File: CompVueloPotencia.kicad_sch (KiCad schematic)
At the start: 2 parts, among them U1 ESP32-S3-WROOM-1

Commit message: another test of updates
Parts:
- added SW1: SW_Push, symbol Switch:SW_Push
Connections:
- net EN: now reaches R1.1
- net EN: now also SW1.2
- net GND: now reaches R1.2
- new net +3V3: SW1.1
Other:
- moved on the sheet: R1

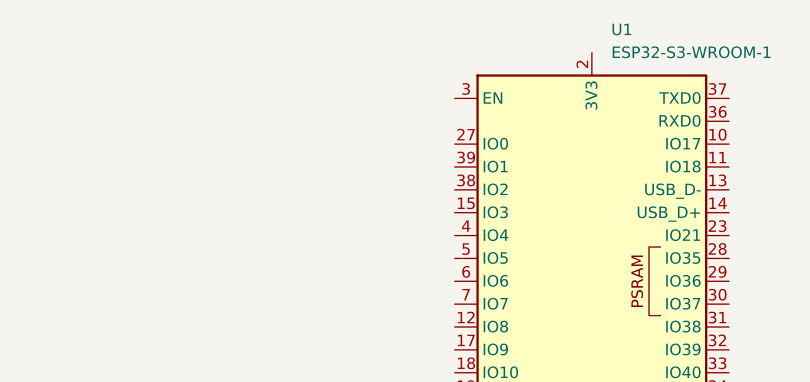
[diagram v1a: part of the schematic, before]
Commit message: last test for updates, only add to gitignore the prl file
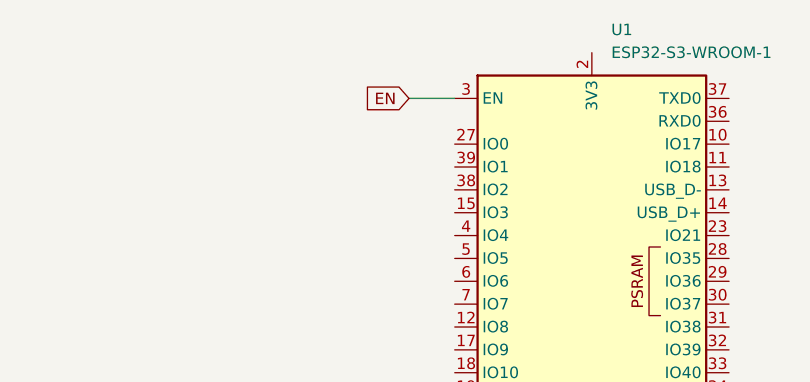
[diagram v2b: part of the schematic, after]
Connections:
- net EN: now also U1.3 (EN)
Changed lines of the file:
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@@
+	(wire
+		(pts
+			(xy 180.34 45.72) (xy 185.42 45.72)
+		)
+		(stroke
+			(width 0)
+			(type default)
+		)
+	)
 	(wire
 		(pts
@@
 		)
 	)
+	(global_label "EN"
+		(shape input)
+		(at 180.34 45.72 180)
+		(fields_autoplaced yes)
+		(effects
+			(font
+				(size 1.27 1.27)
+			)
+			(justify right)
+		)
+		(property "Intersheetrefs" "${INTERSHEET_REFS}"
+			(at 174.8753 45.72 0)
+			(effects
+				(font
+					(size 1.27 1.27)
+				)
+				(justify right)
+				(hide yes)
+			)
+		)
+	)

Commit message: little changes
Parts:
- added C1: .1uF, symbol Device:C_Small
- R1: value R_Small -> 10K
- SW1: value SW_Push -> Reset
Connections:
- net +3V3 is gone; now on net GND: SW1.1
- net GND: now also C1.2; no longer R1.2
- net EN renamed ESP32_EN
- net ESP32_EN: now also R1.2, C1.1; no longer R1.1
- new net +3.3V: R1.1
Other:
- moved on the sheet: R1, SW1
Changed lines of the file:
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@@
 	(paper "A4")
 	(junction
-		(at 80.01 57.15)
+		(at 44.45 48.26)
 		(diameter 0)
 		(color 0 0 0 0)
 	)
-	(wire
-		(pts
-			(xy 80.01 57.15) (xy 80.01 59.69)
-		)
-		(stroke
-			(width 0)
-			(type default)
-		)
-	)
-	(wire
-		(pts
-			(xy 69.85 57.15) (xy 64.77 57.15)
-		)
-		(stroke
-			(width 0)
-			(type default)
-		)
-	)
-	(wire
-		(pts
-			(xy 80.01 64.77) (xy 80.01 66.04)
-		)
-		(stroke
-			(width 0)
-			(type default)
-		)
-	)
-	(wire
-		(pts
-			(xy 64.77 57.15) (xy 64.77 50.8)
+	(junction
+		(at 49.53 39.37)
+		(diameter 0)
+		(color 0 0 0 0)
+	)
+	(junction
+		(at 44.45 39.37)
+		(diameter 0)
+		(color 0 0 0 0)
+	)
+	(wire
+		(pts
+			(xy 49.53 39.37) (xy 54.61 39.37)
+		)
+		(stroke
+			(width 0)
+			(type default)
+		)
+	)
+	(wire
+		(pts
+			(xy 49.53 36.83) (xy 49.53 39.37)
+		)
+		(stroke
+			(width 0)
+			(type default)
+		)
+	)
+	(wire
+		(pts
+			(xy 44.45 39.37) (xy 44.45 41.91)
+		)
+		(stroke
+			(width 0)
+			(type default)
+		)
+	)
+	(wire
+		(pts
+			(xy 44.45 46.99) (xy 44.45 48.26)
+		)
+		(stroke
+			(width 0)
+			(type default)
+		)
+	)
+	(wire
+		(pts
+			(xy 49.53 26.67) (xy 49.53 31.75)
+		)
+		(stroke
+			(width 0)
+			(type default)
+		)
+	)
+	(wire
+		(pts
+			(xy 44.45 48.26) (xy 33.02 48.26)
+		)
+		(stroke
+			(width 0)
+			(type default)
+		)
+	)
+	(wire
+		(pts
+			(xy 44.45 52.07) (xy 44.45 48.26)
+		)
+		(stroke
+			(width 0)
+			(type default)
+		)
+	)
+	(wire
+		(pts
+			(xy 34.29 39.37) (xy 33.02 39.37)
+		)
+		(stroke
+			(width 0)
+			(type default)
+		)
+	)
+	(wire
+		(pts
+			(xy 33.02 39.37) (xy 33.02 48.26)
 		)
 		(stroke
@@
 	(wire
 		(pts
-			(xy 80.01 57.15) (xy 90.17 57.15)
-		)
-		(stroke
-			(width 0)
-			(type default)
-		)
-	)
-	(global_label "EN"
+			(xy 44.45 39.37) (xy 49.53 39.37)
+		)
+		(stroke
+			(width 0)
+			(type default)
+		)
+	)
+	(global_label "ESP32_EN"
 		(shape input)
 		(at 180.34 45.72 180)
@@
 		)
 		(property "Intersheetrefs" "${INTERSHEET_REFS}"
-			(at 174.8753 45.72 0)
+			(at 167.8602 45.72 0)
 			(effects
 				(font
@@
 		)
 	)
-	(global_label "EN"
+	(global_label "ESP32_EN"
 		(shape input)
-		(at 90.17 57.15 0)
+		(at 54.61 39.37 0)
 		(fields_autoplaced yes)
 		(effects
@@
 		)
 		(property "Intersheetrefs" "${INTERSHEET_REFS}"
-			(at 95.6347 57.15 0)
+			(at 67.0898 39.37 0)
 			(effects
 				(font
@@
 	(symbol
 		(lib_id "power:GND")
-		(at 80.01 66.04 0)
+		(at 44.45 52.07 0)
 		(unit 1)
 		(exclude_from_sim no)
@@
 		(fields_autoplaced yes)
 		(property "Reference" "#PWR01"
-			(at 80.01 72.39 0)
+			(at 44.45 58.42 0)
 			(effects
 				(font
@@
 		)
 		(property "Value" "GND"
-			(at 80.01 71.12 0)
+			(at 44.45 57.15 0)
 			(effects
 				(font
@@
 		)
 		(property "Footprint" ""
-			(at 80.01 66.04 0)
+			(at 44.45 52.07 0)
 			(effects
 				(font
@@
 		)
 		(property "Datasheet" ""
-			(at 80.01 66.04 0)
+			(at 44.45 52.07 0)
 			(effects
 				(font
@@
 		)
 		(property "Description" "Power symbol creates a global label with name \"GND\" , ground"
-			(at 80.01 66.04 0)
+			(at 44.45 52.07 0)
 			(effects
 				(font
@@
 	)
 	(symbol
-		(lib_id "power:+3V3")
-		(at 64.77 50.8 0)
+		(lib_id "Device:C_Small")
+		(at 44.45 44.45 0)
 		(unit 1)
 		(exclude_from_sim no)
@@
 		(dnp no)
 		(fields_autoplaced yes)
-		(property "Reference" "#PWR02"
-			(at 64.77 54.61 0)
-			(effects
-				(font
-					(size 1.27 1.27)
-				)
-				(hide yes)
-			)
-		)
-		(property "Value" "+3V3"
-			(at 64.77 45.72 0)
-			(effects
-				(font
-					(size 1.27 1.27)
-				)
+		(property "Reference" "C1"
+			(at 46.99 43.1862 0)
+			(effects
+				(font
+					(size 1.27 1.27)
+				)
+				(justify left)
+			)
+		)
+		(property "Value" ".1uF"
+			(at 46.99 45.7262 0)
+			(effects
+				(font
+					(size 1.27 1.27)
+				)
+				(justify left)
 			)
 		)
 		(property "Footprint" ""
-			(at 64.77 50.8 0)
-			(effects
-				(font
-					(size 1.27 1.27)
-				)
-				(hide yes)
-			)
-		)
-		(property "Datasheet" ""
-			(at 64.77 50.8 0)
-			(effects
-				(font
-					(size 1.27 1.27)
-				)
-				(hide yes)
-			)
-		)
-		(property "Description" "Power symbol creates a global label with name \"+3V3\""
-			(at 64.77 50.8 0)
+			(at 44.45 44.45 0)
+			(effects
+				(font
+					(size 1.27 1.27)
+				)
+				(hide yes)
+			)
+		)
+		(property "Datasheet" "~"
+			(at 44.45 44.45 0)
+			(effects
+				(font
+					(size 1.27 1.27)
+				)
+				(hide yes)
+			)
+		)
+		(property "Description" "Unpolarized capacitor, small symbol"
+			(at 44.45 44.45 0)
 			(effects
 				(font
@@
 		)
 		(pin "1"
+		)
+		(pin "2"
 		)
 		(instances
 			(project ""
 				(path "/a84aba9c-0fb9-4754-89f4-1b118d6ea201"
-					(reference "#PWR02")
+					(reference "C1")
 					(unit 1)
 				)
@@
 	(symbol
 		(lib_id "Switch:SW_Push")
-		(at 74.93 57.15 0)
+		(at 39.37 39.37 0)
 		(unit 1)
 		(exclude_from_sim no)
@@
 		(fields_autoplaced yes)
 		(property "Reference" "SW1"
-			(at 74.93 49.53 0)
-			(effects
-				(font
-					(size 1.27 1.27)
-				)
-			)
-		)
-		(property "Value" "SW_Push"
-			(at 74.93 52.07 0)
+			(at 39.37 31.75 0)
+			(effects
+				(font
+					(size 1.27 1.27)
+				)
+			)
+		)
+		(property "Value" "Reset"
+			(at 39.37 34.29 0)
 			(effects
 				(font
@@
 		)
 		(property "Footprint" ""
-			(at 74.93 52.07 0)
+			(at 39.37 34.29 0)
 			(effects
 				(font
@@
 		)
 		(property "Datasheet" "~"
-			(at 74.93 52.07 0)
+			(at 39.37 34.29 0)
 			(effects
 				(font
@@
 		)
 		(property "Description" "Push button switch, generic, two pins"
-			(at 74.93 57.15 0)
+			(at 39.37 39.37 0)
 			(effects
 				(font
@@
 	(symbol
 		(lib_id "Device:R_Small")
-		(at 80.01 62.23 0)
+		(at 49.53 34.29 0)
 		(unit 1)
 		(exclude_from_sim no)
@@
 		(fields_autoplaced yes)
 		(property "Reference" "R1"
-			(at 82.55 60.9599 0)
+			(at 52.07 33.0199 0)
 			(effects
 				(font
@@
 			)
 		)
-		(property "Value" "R_Small"
-			(at 82.55 63.4999 0)
+		(property "Value" "10K"
+			(at 52.07 35.5599 0)
 			(effects
 				(font
@@
 		)
 		(property "Footprint" ""
-			(at 80.01 62.23 0)
+			(at 49.53 34.29 0)
 			(effects
 				(font
@@
 		)
 		(property "Datasheet" "~"
-			(at 80.01 62.23 0)
+			(at 49.53 34.29 0)
 			(effects
 				(font
@@
 		)
 		(property "Description" "Resistor, small symbol"
-			(at 80.01 62.23 0)
+			(at 49.53 34.29 0)
 			(effects
 				(font
@@
 		)
 		(instances
-			(project ""
+			(project "CompVueloPotencia"
 				(path "/a84aba9c-0fb9-4754-89f4-1b118d6ea201"
 					(reference "R1")
@@
 					(unit 1)
 				)
+			)
+		)
+	)
+	(symbol
+		(lib_id "power:+3.3V")
+		(at 49.53 26.67 0)
+		(unit 1)
+		(exclude_from_sim no)
+		(in_bom yes)
+		(on_board yes)
+		(dnp no)
+		(fields_autoplaced yes)
+		(property "Reference" "#PWR02"
+			(at 49.53 30.48 0)
+			(effects
+				(font
+					(size 1.27 1.27)
+				)
+				(hide yes)
+			)
+		)
+		(property "Value" "+3.3V"
+			(at 49.53 21.59 0)
+			(effects
+				(font
+					(size 1.27 1.27)
+				)
+			)
+		)
+		(property "Footprint" ""
+			(at 49.53 26.67 0)
+			(effects
+				(font
+					(size 1.27 1.27)
+				)
+				(hide yes)
+			)
+		)
+		(property "Datasheet" ""
+			(at 49.53 26.67 0)
+			(effects
+				(font
+					(size 1.27 1.27)
+				)
+				(hide yes)
+			)
+		)
+		(property "Description" "Power symbol creates a global label with name \"+3.3V\""
+			(at 49.53 26.67 0)
+			(effects
+				(font
+					(size 1.27 1.27)
+				)
+				(hide yes)
+			)
+		)
+		(pin "1"
+		)
+		(instances
+			(project ""
+				(path "/a84aba9c-0fb9-4754-89f4-1b118d6ea201"
+					(reference "#PWR02")
+					(unit 1)
+				)
